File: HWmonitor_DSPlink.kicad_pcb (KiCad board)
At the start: 2 copper layers, 56 x 66 mm, 99 parts, among them J1 Mini USB - Type B, J2 IDC-Header 2x4, T1 760390014, U1 FT232RL, U10 OPA197xDBV, U11 OPA197xDBV, U12 USBLC6-2SC6, U2 ISO7830DWW, U3 ISO7821DWW, U4 SN6501DBVR, U5 TL431BCDBZ, U6 AD5324ARMZ, U7 TLV70450DBVT, U8 OPA197xDBV, U9 OPA197xDBV, X1 Conn_Coaxial, X2 Conn_Coaxial, X3 Conn_Coaxial, X4 Conn_Coaxial

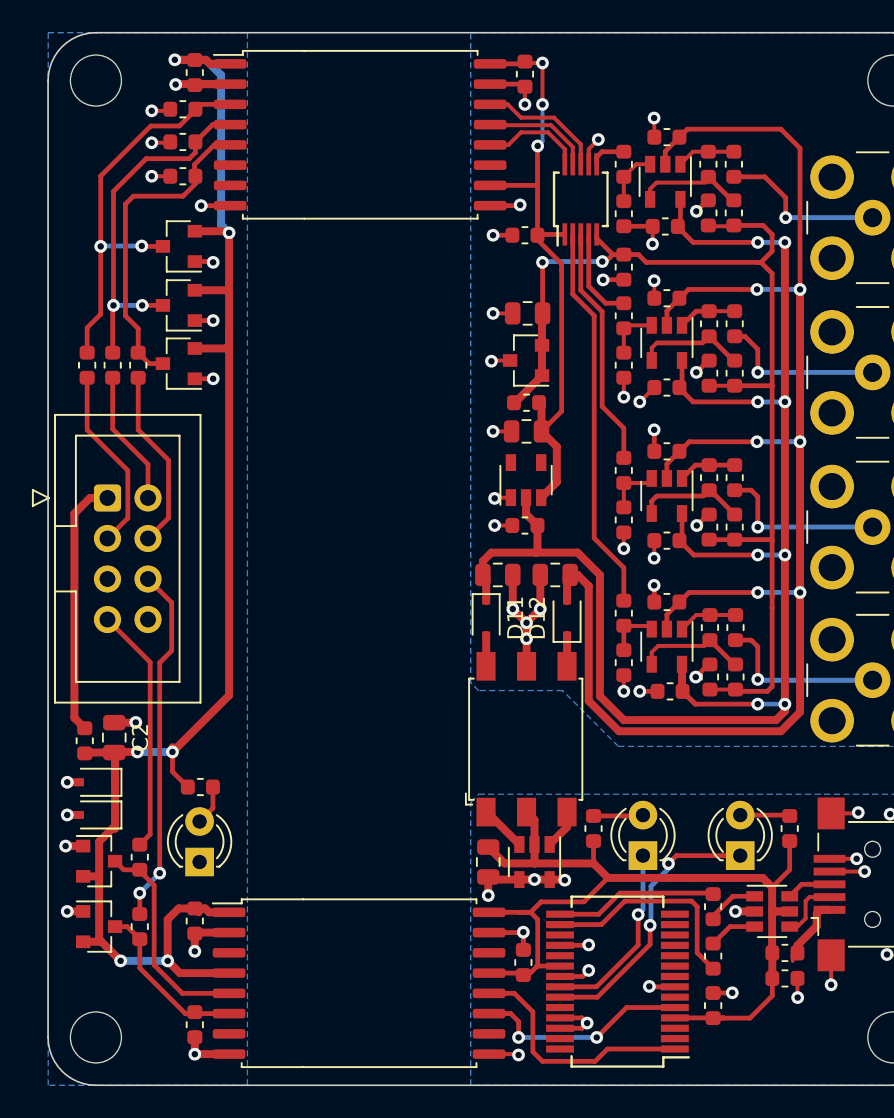
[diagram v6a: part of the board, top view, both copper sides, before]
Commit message: modified layout ftdi chip, added 3.3V capacitor
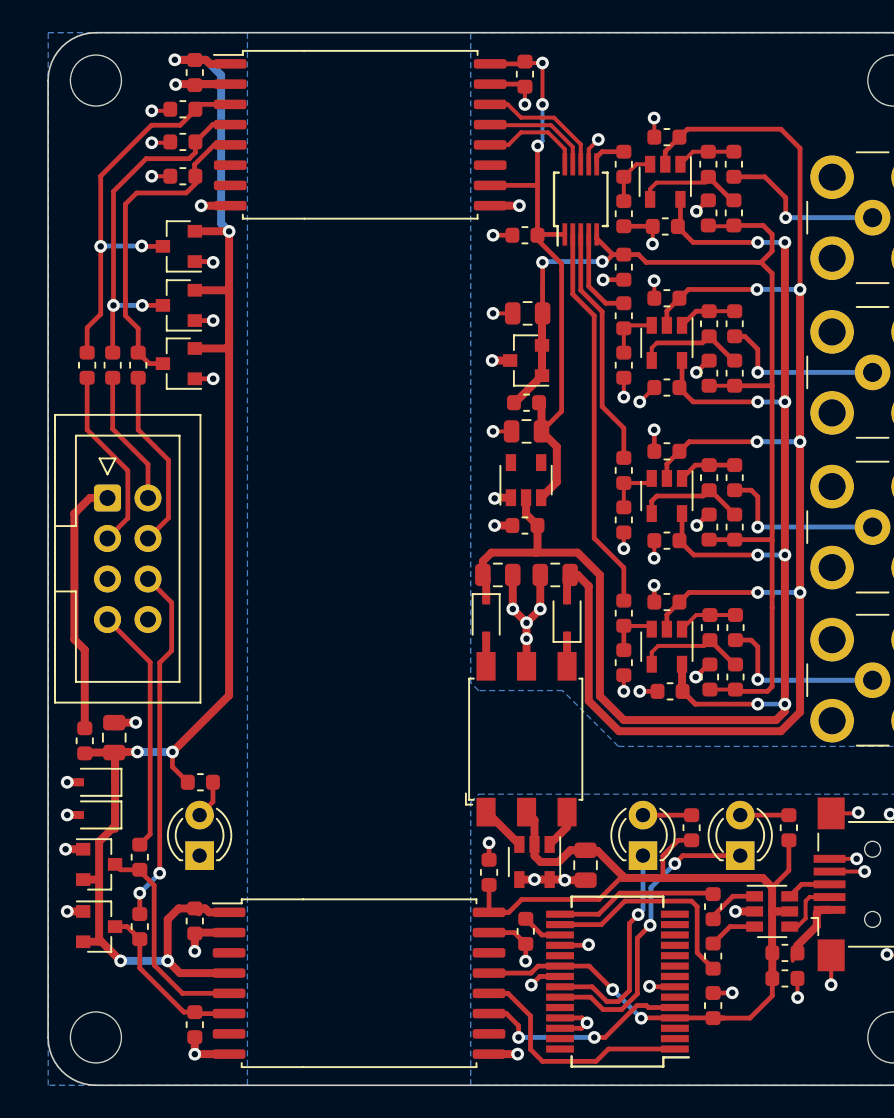
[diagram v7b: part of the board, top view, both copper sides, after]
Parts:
- added C36: 100nF/50V, Capacitor_SMD:C_0603_1608Metric, F.Cu at (147.4, 114.2)
- J1: value Mini USB - Type B -> Mini USB-B
- L1: value 1k @100MHz -> 1k@100MHz
- moved R9 6.15 mm to (157.8, 107.7)
- moved C9 6.10 mm to (151.1, 110.0)
- moved C12 6.05 mm to (145.1, 110.5)
- moved D5 0.40 mm to (126.9, 109.4)
- moved R4 0.30 mm to (127.0, 104.8)
- moved D1 0.20 mm to (120.6, 110.0)
- moved R8 0.07 mm to (163.9, 107.7)
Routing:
- net +5VA: track 69.9 -> 75.2 mm, vias 0 -> 2
- net Net-(C36-Pad2): track 0.00 -> 2.57 mm
- net /LED_RX: track 11.7 -> 13.8 mm
- net /LED_TX: track 17.5 -> 19.2 mm
- net /TXD: track 16.4 -> 15.2 mm
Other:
- rule pad_to_mask_clearance: 0.05 -> 0.025

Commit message: last modifications, documents generated
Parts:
- moved X2 0.10 mm to (169.1, 88.7)
- moved X3 0.10 mm to (169.1, 79.0)
- moved X4 0.10 mm to (169.1, 69.3)
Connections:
- J1 pad 4: GNDA -> Net-(J1-Pad4)
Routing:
- net GNDA: track 35.0 -> 33.6 mm
- net +5V: track 39.2 -> 39.0 mm, vias 3 -> 2
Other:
- board text added: "DSP DEBUG TOOL HW1.0"
